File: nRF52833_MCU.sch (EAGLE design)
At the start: 44 parts, among them IC1 SKY13415-485LF, J1 282834-2, J100 DEBUG_CONNECTOR, J2 282834-2, J3 282834-2, U1 nRF52833-QIAA, U3 BQ25570RGRR, X1 32MHz, X2 32.768kHz, X3 22-23-2031

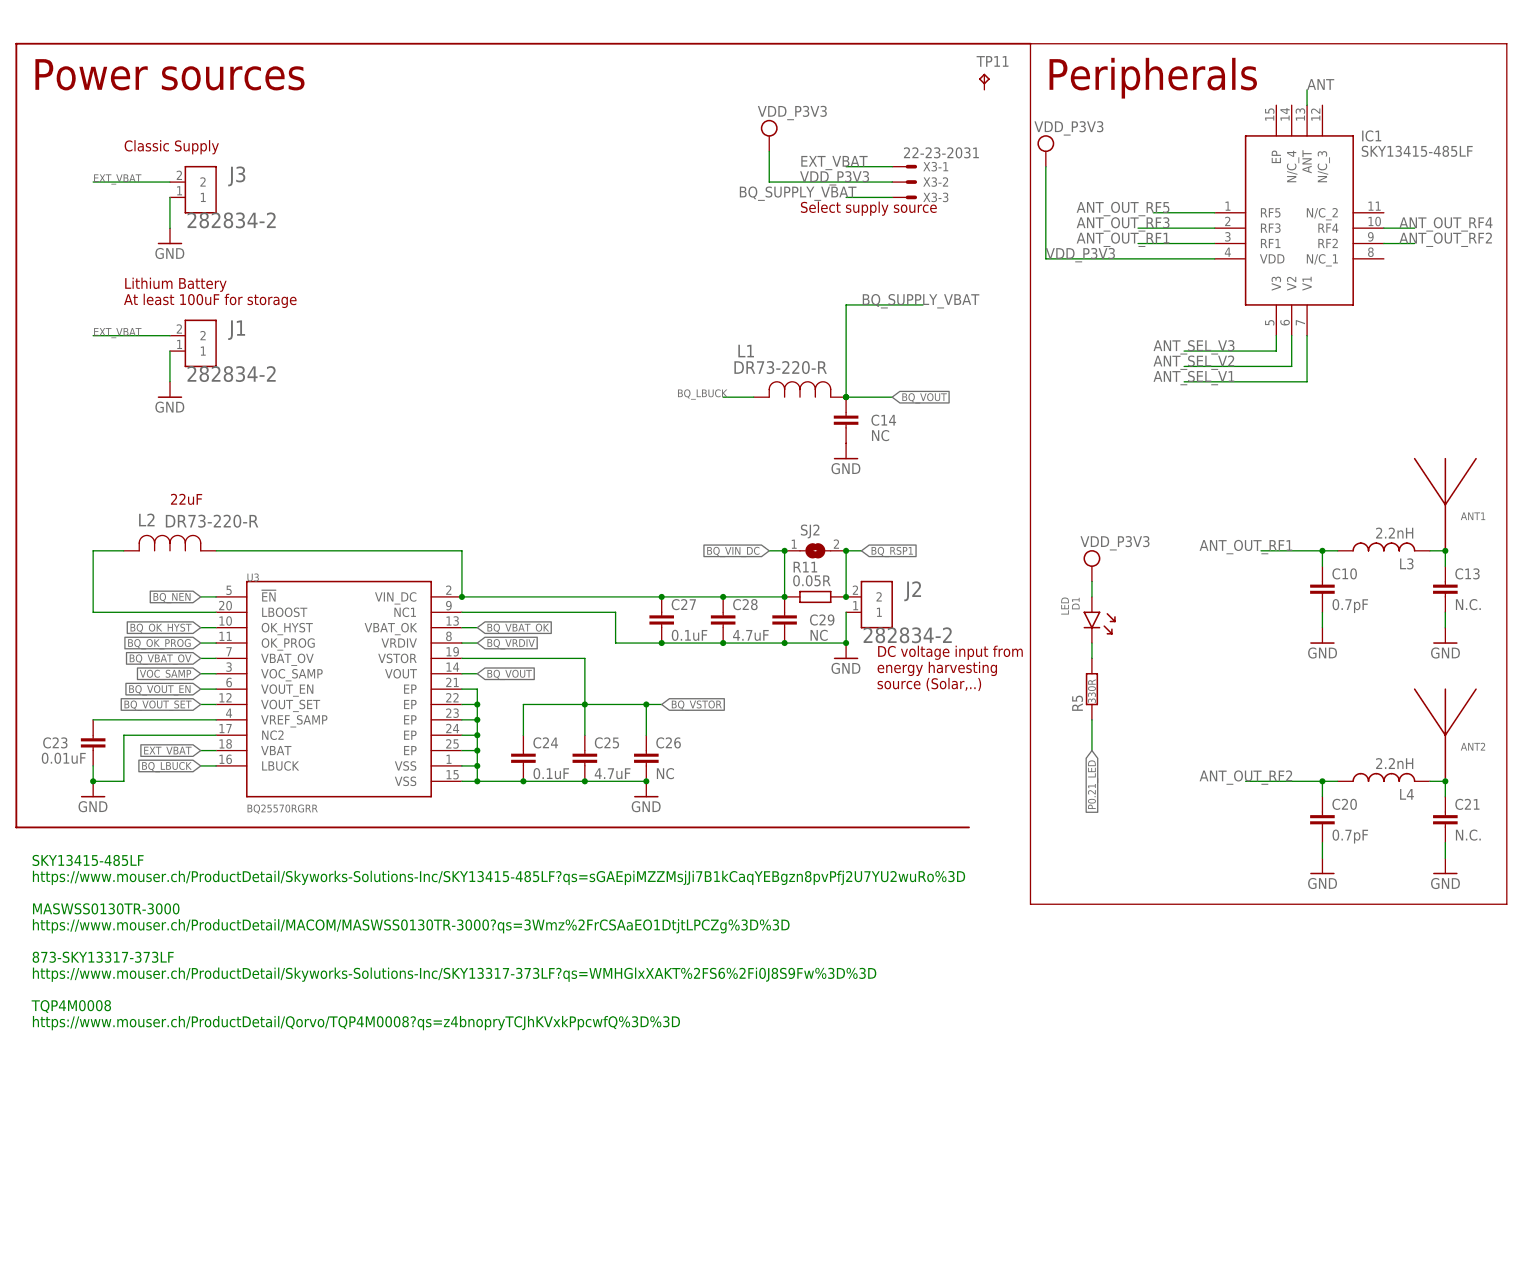
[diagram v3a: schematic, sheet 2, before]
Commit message: Separate the power and the antennas
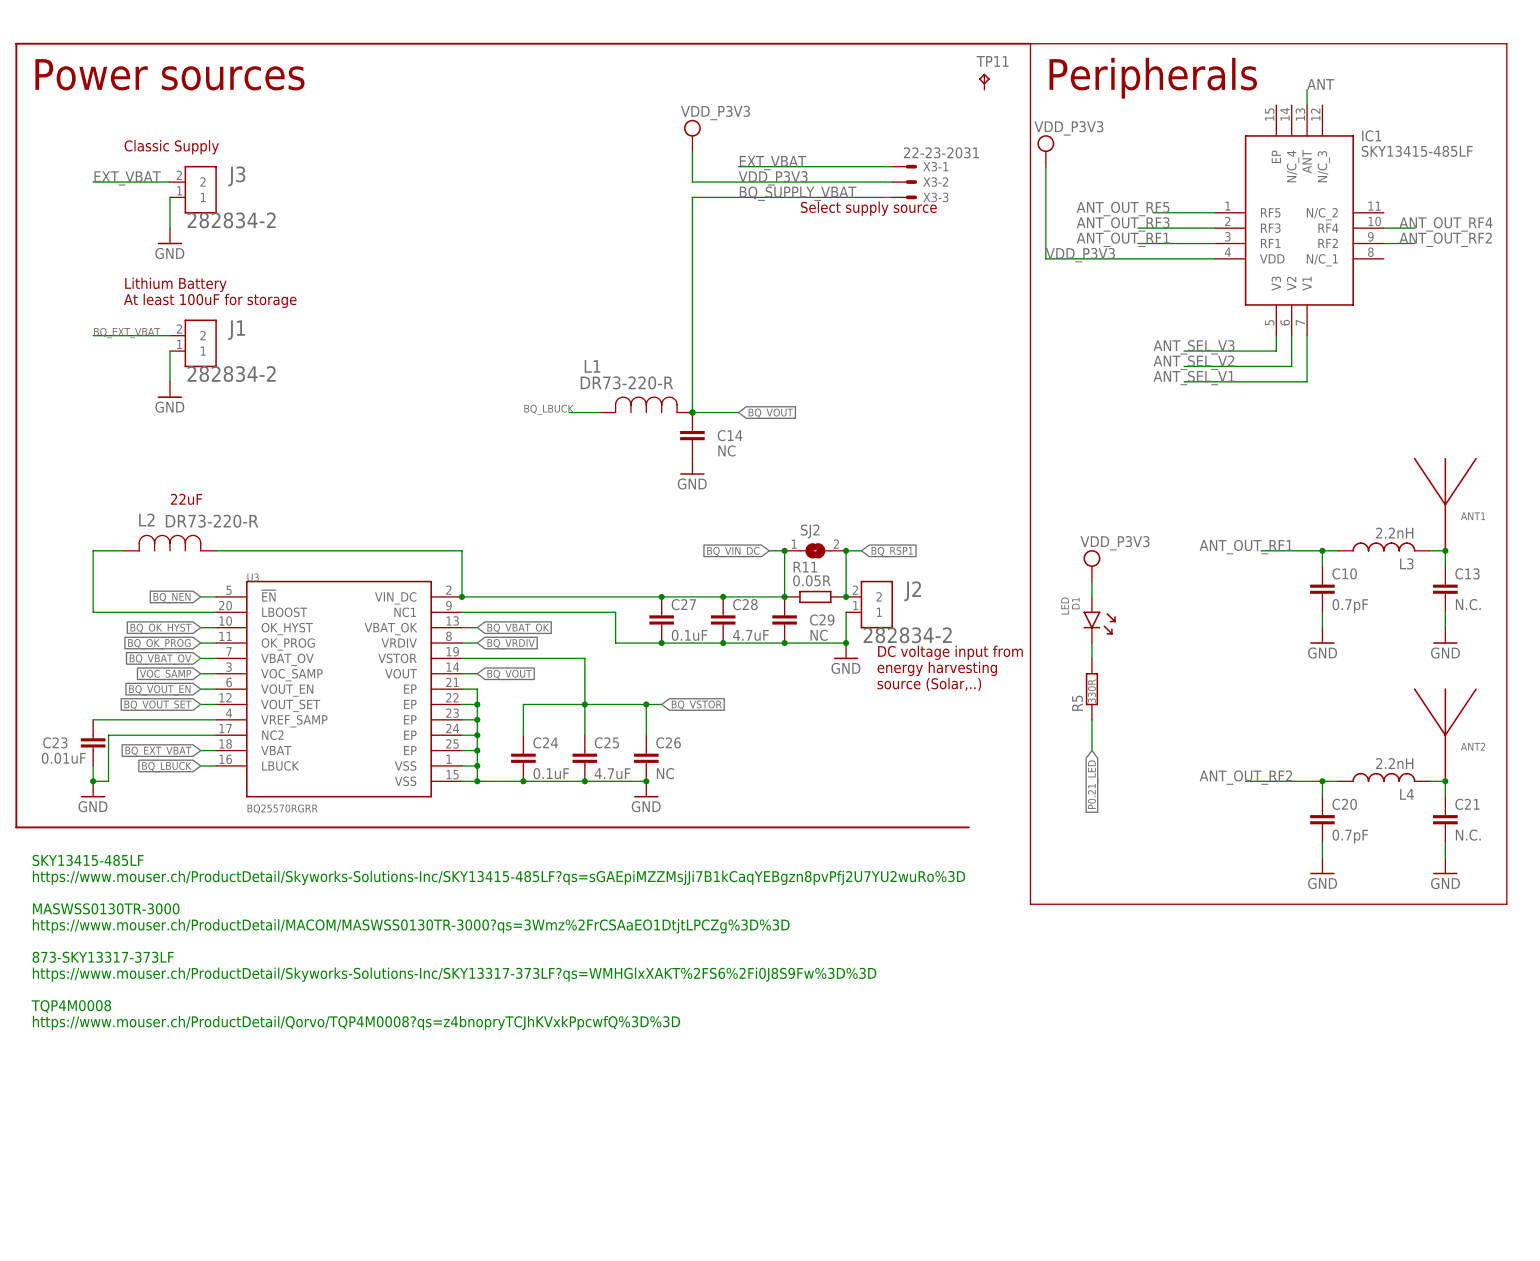
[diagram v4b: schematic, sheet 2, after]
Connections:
- new net BQ_EXT_VBAT: J1.2, U3.VBAT
- net EXT_VBAT: no longer J1.2, U3.VBAT
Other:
- moved on the sheet: C14, L1
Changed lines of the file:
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@@
 <attribute name="VALUE" x="136.144" y="68.961" size="1.778" layer="96"/>
 </instance>
-<instance part="L1" gate="A" x="127" y="109.22" smashed="yes">
-<attribute name="NAME" x="124.18138125" y="115.799990625" size="2.08351875" layer="95" ratio="10" rot="SR0"/>
-<attribute name="VALUE" x="123.52245" y="113.07551875" size="2.08573125" layer="96" ratio="10" rot="SR0"/>
-</instance>
-<instance part="GND26" gate="1" x="142.24" y="99.06" smashed="yes">
-<attribute name="VALUE" x="139.7" y="96.52" size="1.778" layer="96"/>
-</instance>
-<instance part="C14" gate="C$1" x="142.24" y="106.68" smashed="yes">
-<attribute name="NAME" x="146.304" y="104.521" size="1.778" layer="95"/>
-<attribute name="VALUE" x="146.304" y="101.981" size="1.778" layer="96"/>
+<instance part="L1" gate="A" x="101.6" y="106.68" smashed="yes">
+<attribute name="NAME" x="98.78138125" y="113.259990625" size="2.08351875" layer="95" ratio="10" rot="SR0"/>
+<attribute name="VALUE" x="98.12245" y="110.53551875" size="2.08573125" layer="96" ratio="10" rot="SR0"/>
+</instance>
+<instance part="GND26" gate="1" x="116.84" y="96.52" smashed="yes">
+<attribute name="VALUE" x="114.3" y="93.98" size="1.778" layer="96"/>
+</instance>
+<instance part="C14" gate="C$1" x="116.84" y="104.14" smashed="yes">
+<attribute name="NAME" x="120.904" y="101.981" size="1.778" layer="95"/>
+<attribute name="VALUE" x="120.904" y="99.441" size="1.778" layer="96"/>
 </instance>
 <instance part="J1" gate="G$1" x="35.56" y="116.84" smashed="yes" rot="R180">
@@
 <attribute name="VALUE" x="27.94" y="132.08" size="1.778" layer="96"/>
 </instance>
-<instance part="VDD_NRF9" gate="G$1" x="129.54" y="152.4" smashed="yes">
-<attribute name="VALUE" x="127.635" y="155.575" size="1.778" layer="96"/>
+<instance part="VDD_NRF9" gate="G$1" x="116.84" y="152.4" smashed="yes">
+<attribute name="VALUE" x="114.935" y="155.575" size="1.778" layer="96"/>
 </instance>
 <instance part="X3" gate="-1" x="152.4" y="147.32" smashed="yes">
@@
 <pinref part="VDD_NRF9" gate="G$1" pin="VCC"/>
 <pinref part="X3" gate="-2" pin="S"/>
-<wire x1="129.54" y1="149.86" x2="129.54" y2="144.78" width="0.1524" layer="91"/>
-<wire x1="129.54" y1="144.78" x2="149.86" y2="144.78" width="0.1524" layer="91"/>
-<label x="134.62" y="144.78" size="1.778" layer="95"/>
+<wire x1="116.84" y1="149.86" x2="116.84" y2="144.78" width="0.1524" layer="91"/>
+<wire x1="116.84" y1="144.78" x2="149.86" y2="144.78" width="0.1524" layer="91"/>
+<label x="124.46" y="144.78" size="1.778" layer="95"/>
 </segment>
 <segment>
@@
 <wire x1="17.78" y1="48.26" x2="17.78" y2="45.72" width="0.1524" layer="91"/>
 <pinref part="C23" gate="C$1" pin="2"/>
-<wire x1="22.86" y1="45.72" x2="22.86" y2="53.34" width="0.1524" layer="91"/>
+<wire x1="20.32" y1="45.72" x2="20.32" y2="53.34" width="0.1524" layer="91"/>
 <pinref part="U3" gate="G$1" pin="NC2"/>
-<wire x1="38.1" y1="53.34" x2="22.86" y2="53.34" width="0.1524" layer="91"/>
-<wire x1="17.78" y1="45.72" x2="22.86" y2="45.72" width="0.1524" layer="91"/>
+<wire x1="38.1" y1="53.34" x2="20.32" y2="53.34" width="0.1524" layer="91"/>
+<wire x1="17.78" y1="45.72" x2="20.32" y2="45.72" width="0.1524" layer="91"/>
 <junction x="17.78" y="45.72"/>
 </segment>
@@
 </segment>
 </net>
-<net name="EXT_VBAT" class="0">
+<net name="BQ_EXT_VBAT" class="0">
 <segment>
 <pinref part="U3" gate="G$1" pin="VBAT"/>
@@
 <wire x1="30.48" y1="119.38" x2="17.78" y2="119.38" width="0.1524" layer="91"/>
 </segment>
-<segment>
-<pinref part="J3" gate="G$1" pin="2"/>
-<label x="17.78" y="144.78" size="1.27" layer="95"/>
-<wire x1="30.48" y1="144.78" x2="17.78" y2="144.78" width="0.1524" layer="91"/>
-</segment>
-<segment>
-<wire x1="142.24" y1="147.32" x2="149.86" y2="147.32" width="0.1524" layer="91"/>
-<label x="134.62" y="147.32" size="1.778" layer="95"/>
-<pinref part="X3" gate="-1" pin="S"/>
-</segment>
 </net>
 <net name="BQ_VBAT_OK" class="0">
@@
 <segment>
 <pinref part="L1" gate="A" pin="2"/>
-<wire x1="121.92" y1="109.22" x2="127" y2="109.22" width="0.1524" layer="91"/>
-<label x="114.3" y="109.22" size="1.27" layer="95"/>
+<wire x1="96.52" y1="106.68" x2="101.6" y2="106.68" width="0.1524" layer="91"/>
+<label x="88.9" y="106.68" size="1.27" layer="95"/>
 </segment>
 </net>
@@
 </segment>
 <segment>
-<label x="149.86" y="109.22" size="1.27" layer="95" xref="yes"/>
+<label x="124.46" y="106.68" size="1.27" layer="95" xref="yes"/>
 </segment>
 </net>
@@
 <pinref part="L1" gate="A" pin="1"/>
 <pinref part="C14" gate="C$1" pin="1"/>
-<wire x1="142.24" y1="109.22" x2="142.24" y2="124.46" width="0.1524" layer="91"/>
-<junction x="142.24" y="109.22"/>
-<wire x1="149.86" y1="109.22" x2="142.24" y2="109.22" width="0.1524" layer="91"/>
-<junction x="142.24" y="109.22"/>
-<wire x1="142.24" y1="124.46" x2="154.94" y2="124.46" width="0.1524" layer="91"/>
-<label x="144.78" y="124.46" size="1.778" layer="95"/>
-</segment>
-<segment>
-<wire x1="142.24" y1="142.24" x2="149.86" y2="142.24" width="0.1524" layer="91"/>
+<wire x1="116.84" y1="106.68" x2="116.84" y2="142.24" width="0.1524" layer="91"/>
+<junction x="116.84" y="106.68"/>
+<wire x1="124.46" y1="106.68" x2="116.84" y2="106.68" width="0.1524" layer="91"/>
+<junction x="116.84" y="106.68"/>
 <label x="124.46" y="142.24" size="1.778" layer="95"/>
 <pinref part="X3" gate="-3" pin="S"/>
-</segment>
-</net>
+<wire x1="116.84" y1="142.24" x2="149.86" y2="142.24" width="0.1524" layer="91"/>
+</segment>
+</net>
+<net name="EXT_VBAT" class="0">
+<segment>
+<pinref part="J3" gate="G$1" pin="2"/>
+<wire x1="30.48" y1="144.78" x2="17.78" y2="144.78" width="0.1524" layer="91"/>
+<label x="17.78" y="144.78" size="1.778" layer="95"/>
+</segment>
+<segment>
+<pinref part="X3" gate="-1" pin="S"/>
+<wire x1="149.86" y1="147.32" x2="124.46" y2="147.32" width="0.1524" layer="91"/>
+<label x="124.46" y="147.32" size="1.778" layer="95"/>
+</segment>
+</net>

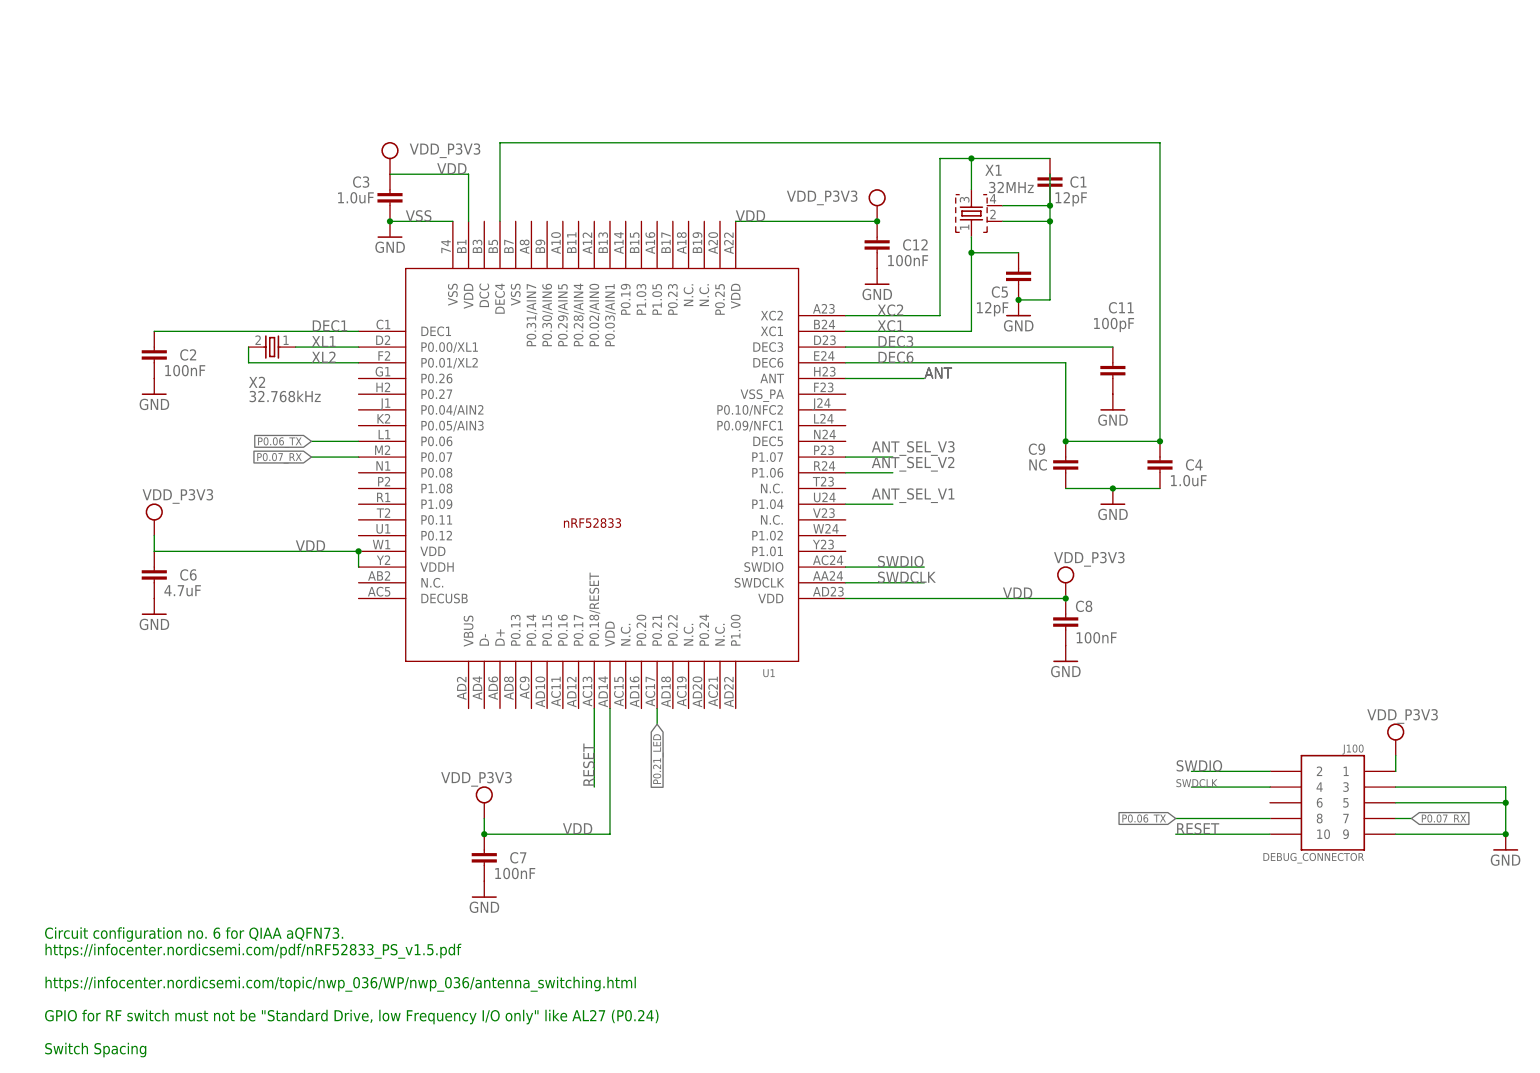
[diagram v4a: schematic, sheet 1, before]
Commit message: Schematic: Move devices
Signed-off-by: Florian Depraz <florian.depraz@outlook.com>
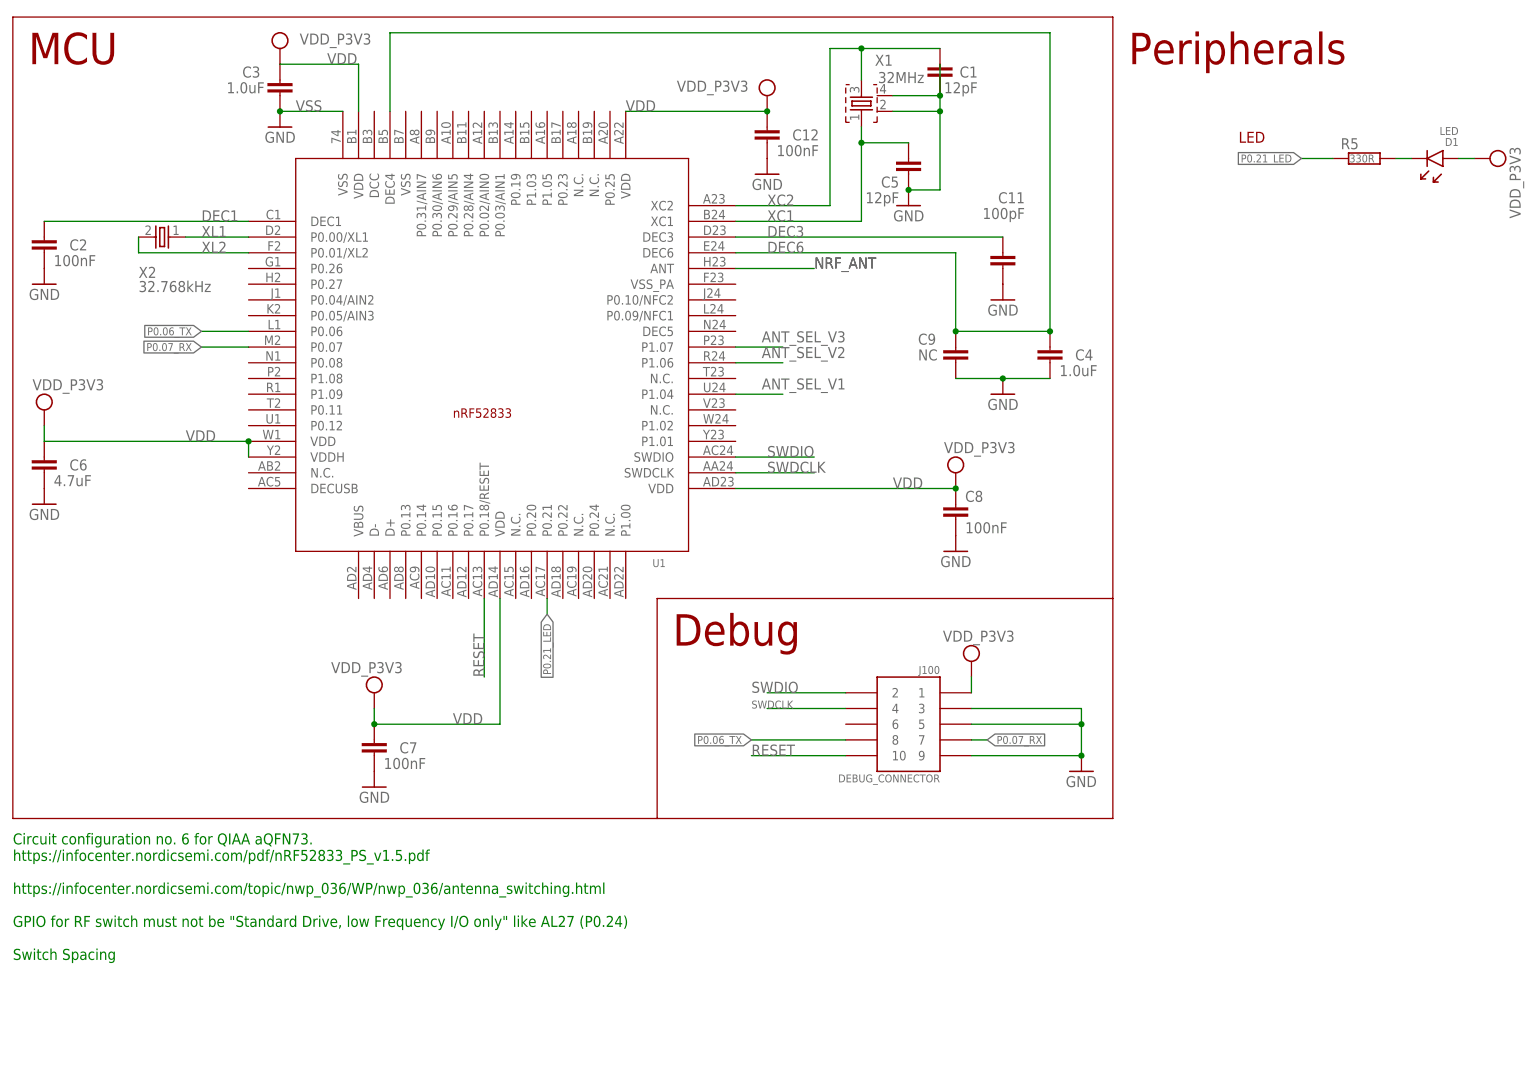
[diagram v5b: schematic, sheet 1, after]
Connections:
- net ANT renamed NRF_ANT
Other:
- note added: "Antennas"
- note added: "Debug"
- note added: "LED"
- note added: "MCU"
- moved on the sheet: ANT1, ANT2, C1, C10, C11, C12, C13, C14, C2, C20, C21, C23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
